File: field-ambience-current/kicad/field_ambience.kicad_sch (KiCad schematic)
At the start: 0 parts

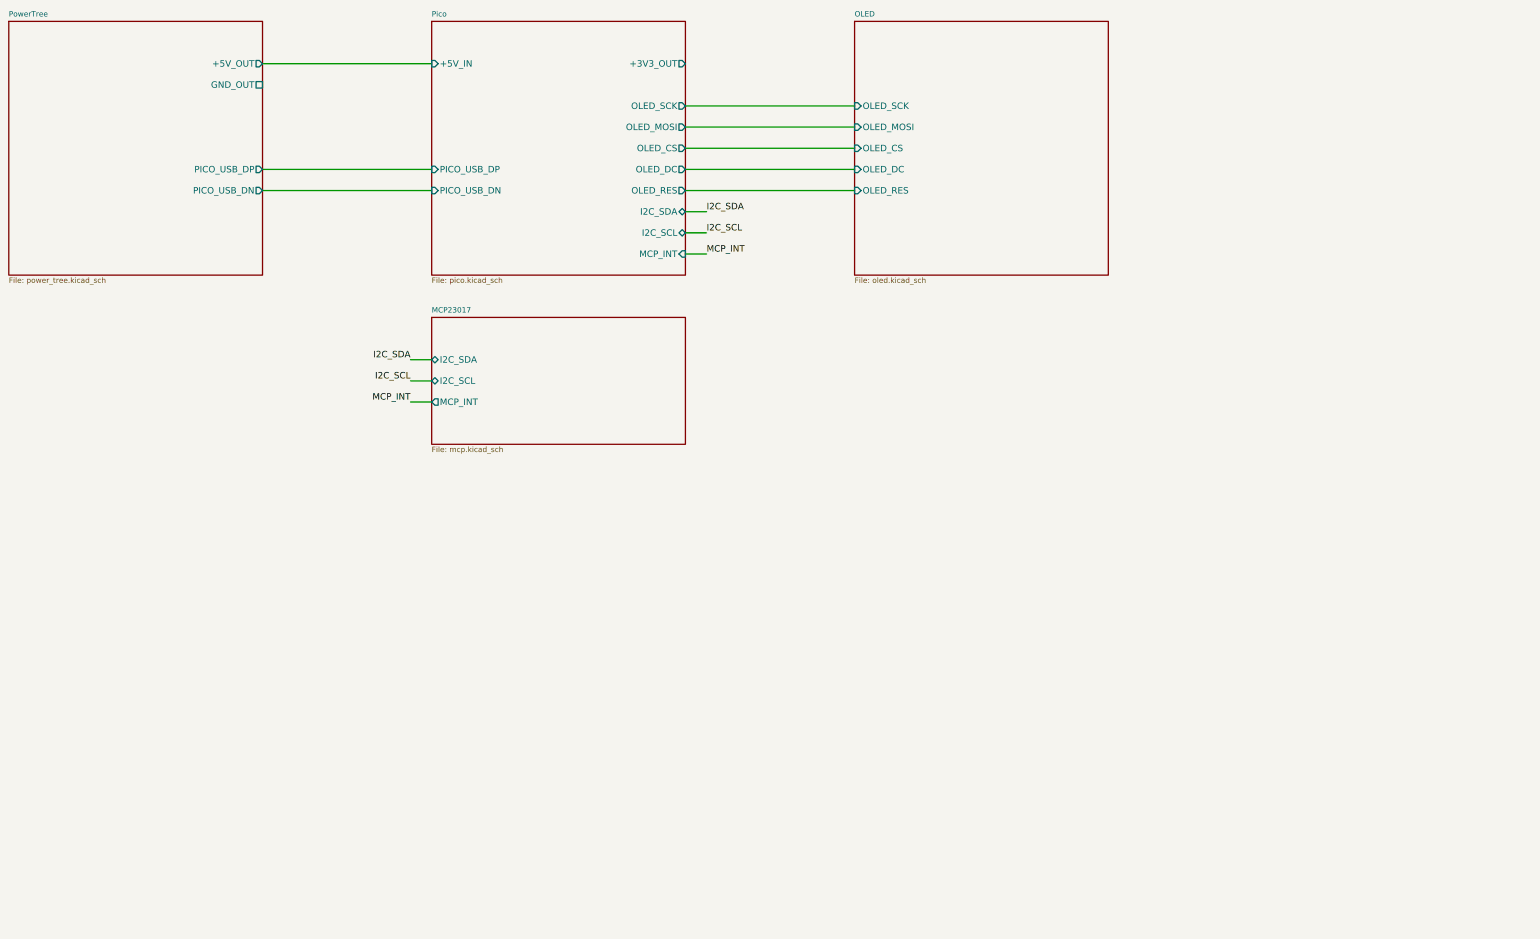
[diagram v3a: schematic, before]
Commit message: Add Sheet 5 (4x EC11 Encoder + RC-Debounce) per SPEC v0.6 §5/§M4
4 EC11-Encoder mit Push-Switch + Pull-Ups + Debounce-Caps:
- EN1 Drive (GP10/11/12)
- EN2 Brightness (GP13/14/15)
- EN3 Display (GP16/17/18)
- EN4 Volume (GP19/20/21)

Per encoder:
- A-Pin: R pull-up 10k zu +3V3, C debounce 100nF zu GND (v0.6 M4 Fix)
- B-Pin: R pull-up 10k, C debounce 100nF
- C-Pin: direkt zu GND (Common)
- SW1-Pin: R pull-up 10k, Hier-Output zu Pico
- SW2-Pin: direkt zu GND

BOM Sheet 5: 12× R 10k (8 für A/B-Pull-Ups R7-R14 + 4 für SW R15-R18),
8× C 100nF (Debounce C10-C17), 4× EC11 Encoder.

Root sheet umstrukturiert für Layout-Platz:
- Pico-Box erweitert von (60, 60) auf (60, 130) für 12 zusätzliche
  Encoder-Pins auf rechter Seite (y=110-165)
- MCP-Box von (130, 110) nach (130, 200) verschoben um Pico-Expansion
  Platz zu machen; I2C/INT-Labels entsprechend bei y=210-220 jetzt
- Encoder-Box bei (230, 105) size (60, 70) mit 12 input pins
- 12 direkte Wires Pico→Encoder bei y=110-165

Analyzer: 0 funktionale Errors (3 VM-001 false-positives unverändert),
23 warnings (von 35 gefallen, da Encoder-Signale jetzt 2-pin nets sind).
61 components total, 70 nets, 16 caps + 20 resistors + 16 switches.

Alle 4 EN1-EN4 pin_nets verifiziert via analyzer:
  Pin 1 (A): correct net (DRIVE_A / BRIGHT_A / DISPLAY_A / VOL_A)
  Pin 2 (B): correct net
  Pin 3 (C): GND
  Pin 4 (SW1): correct SW net
  Pin 5 (SW2): GND
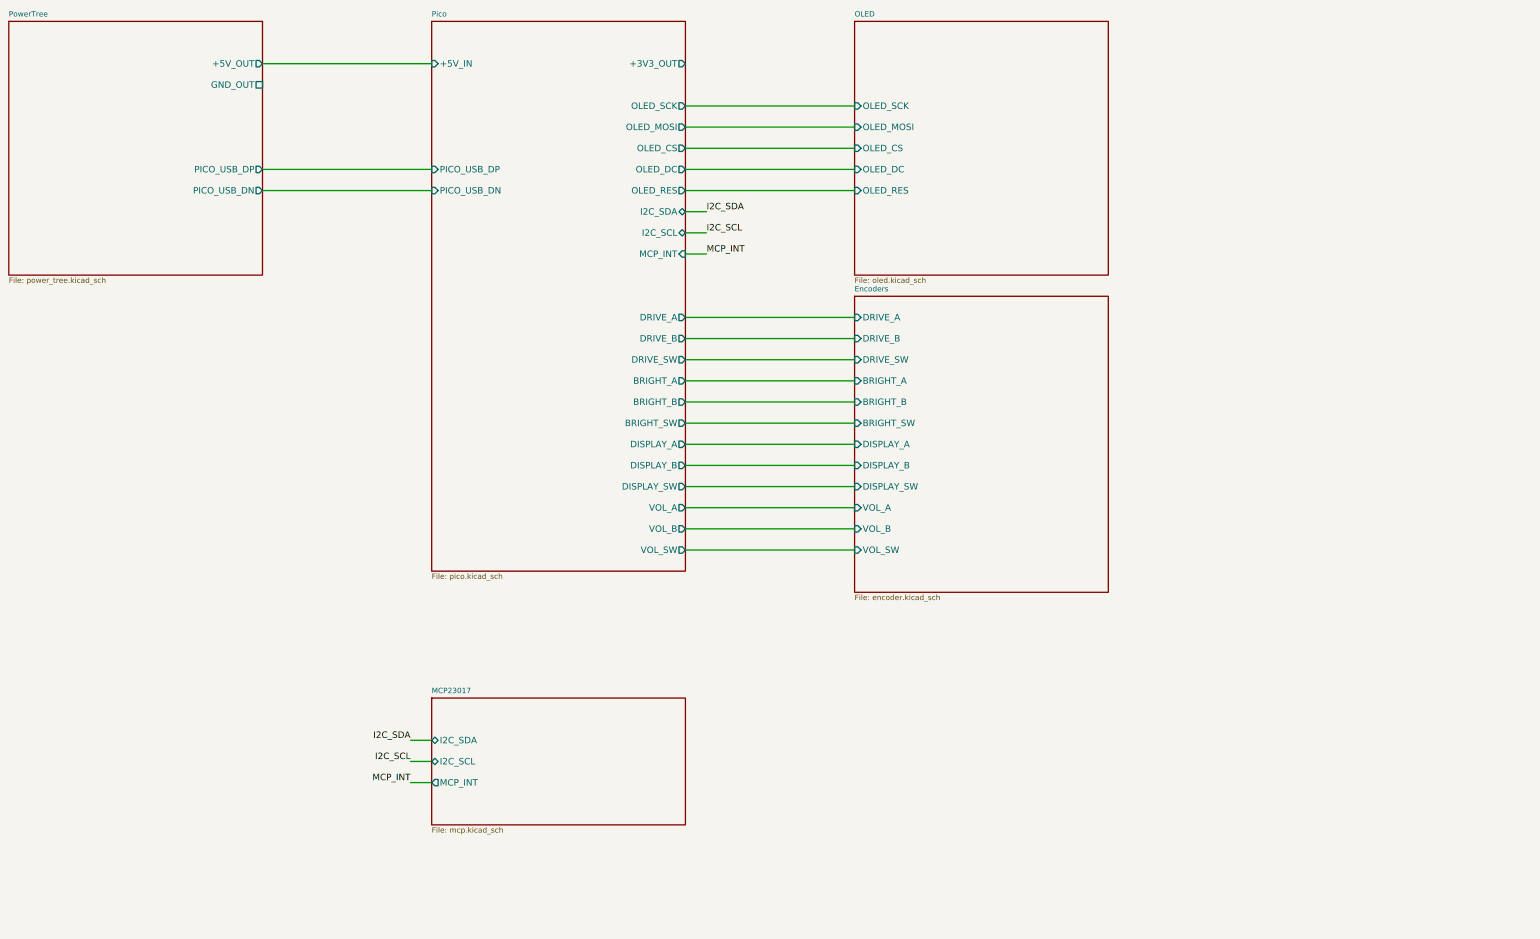
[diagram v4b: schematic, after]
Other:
- added sheet Encoders (encoder.kicad_sch)
- sheet Pico ports: added BRIGHT_A, BRIGHT_B, BRIGHT_SW, DISPLAY_A, DISPLAY_B, DISPLAY_SW, DRIVE_A, DRIVE_B, DRIVE_SW, VOL_A, VOL_B, VOL_SW; removed none
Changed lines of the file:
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@@
       (effects (font (size 1.524 1.524)) (justify right))
 ))
-  (sheet (at 130 40) (size 60 60) (fields_autoplaced)
+  (sheet (at 130 40) (size 60 130) (fields_autoplaced)
     (stroke (width 0.1524) (type solid))
     (fill (color 0 0 0 0.0000))
     (property "Sheetname" "Pico" (at 130 39 0)
       (effects (font (size 1.27 1.27)) (justify left bottom)))
-    (property "Sheetfile" "pico.kicad_sch" (at 130 100.5 0)
+    (property "Sheetfile" "pico.kicad_sch" (at 130 170.5 0)
       (effects (font (size 1.27 1.27)) (justify left top)))
     (pin "+5V_IN" input (at 130 50 180)
@@
     (pin "MCP_INT" input (at 190 95 0)
       (effects (font (size 1.524 1.524)) (justify right))
+)
+    (pin "DRIVE_A" output (at 190 110 0)
+      (effects (font (size 1.524 1.524)) (justify right))
+)
+    (pin "DRIVE_B" output (at 190 115 0)
+      (effects (font (size 1.524 1.524)) (justify right))
+)
+    (pin "DRIVE_SW" output (at 190 120 0)
+      (effects (font (size 1.524 1.524)) (justify right))
+)
+    (pin "BRIGHT_A" output (at 190 125 0)
+      (effects (font (size 1.524 1.524)) (justify right))
+)
+    (pin "BRIGHT_B" output (at 190 130 0)
+      (effects (font (size 1.524 1.524)) (justify right))
+)
+    (pin "BRIGHT_SW" output (at 190 135 0)
+      (effects (font (size 1.524 1.524)) (justify right))
+)
+    (pin "DISPLAY_A" output (at 190 140 0)
+      (effects (font (size 1.524 1.524)) (justify right))
+)
+    (pin "DISPLAY_B" output (at 190 145 0)
+      (effects (font (size 1.524 1.524)) (justify right))
+)
+    (pin "DISPLAY_SW" output (at 190 150 0)
+      (effects (font (size 1.524 1.524)) (justify right))
+)
+    (pin "VOL_A" output (at 190 155 0)
+      (effects (font (size 1.524 1.524)) (justify right))
+)
+    (pin "VOL_B" output (at 190 160 0)
+      (effects (font (size 1.524 1.524)) (justify right))
+)
+    (pin "VOL_SW" output (at 190 165 0)
+      (effects (font (size 1.524 1.524)) (justify right))
 ))
   (sheet (at 230 40) (size 60 60) (fields_autoplaced)
@@
       (effects (font (size 1.524 1.524)) (justify left))
 ))
-  (sheet (at 130 110) (size 60 30) (fields_autoplaced)
+  (sheet (at 130 200) (size 60 30) (fields_autoplaced)
     (stroke (width 0.1524) (type solid))
     (fill (color 0 0 0 0.0000))
-    (property "Sheetname" "MCP23017" (at 130 109 0)
+    (property "Sheetname" "MCP23017" (at 130 199 0)
       (effects (font (size 1.27 1.27)) (justify left bottom)))
-    (property "Sheetfile" "mcp.kicad_sch" (at 130 140.5 0)
+    (property "Sheetfile" "mcp.kicad_sch" (at 130 230.5 0)
       (effects (font (size 1.27 1.27)) (justify left top)))
-    (pin "I2C_SDA" bidirectional (at 130 120 180)
+    (pin "I2C_SDA" bidirectional (at 130 210 180)
       (effects (font (size 1.524 1.524)) (justify left))
 )
-    (pin "I2C_SCL" bidirectional (at 130 125 180)
+    (pin "I2C_SCL" bidirectional (at 130 215 180)
       (effects (font (size 1.524 1.524)) (justify left))
 )
-    (pin "MCP_INT" output (at 130 130 180)
+    (pin "MCP_INT" output (at 130 220 180)
+      (effects (font (size 1.524 1.524)) (justify left))
+))
+  (sheet (at 230 105) (size 60 70) (fields_autoplaced)
+    (stroke (width 0.1524) (type solid))
+    (fill (color 0 0 0 0.0000))
+    (property "Sheetname" "Encoders" (at 230 104 0)
+      (effects (font (size 1.27 1.27)) (justify left bottom)))
+    (property "Sheetfile" "encoder.kicad_sch" (at 230 175.5 0)
+      (effects (font (size 1.27 1.27)) (justify left top)))
+    (pin "DRIVE_A" input (at 230 110 180)
+      (effects (font (size 1.524 1.524)) (justify left))
+)
+    (pin "DRIVE_B" input (at 230 115 180)
+      (effects (font (size 1.524 1.524)) (justify left))
+)
+    (pin "DRIVE_SW" input (at 230 120 180)
+      (effects (font (size 1.524 1.524)) (justify left))
+)
+    (pin "BRIGHT_A" input (at 230 125 180)
+      (effects (font (size 1.524 1.524)) (justify left))
+)
+    (pin "BRIGHT_B" input (at 230 130 180)
+      (effects (font (size 1.524 1.524)) (justify left))
+)
+    (pin "BRIGHT_SW" input (at 230 135 180)
+      (effects (font (size 1.524 1.524)) (justify left))
+)
+    (pin "DISPLAY_A" input (at 230 140 180)
+      (effects (font (size 1.524 1.524)) (justify left))
+)
+    (pin "DISPLAY_B" input (at 230 145 180)
+      (effects (font (size 1.524 1.524)) (justify left))
+)
+    (pin "DISPLAY_SW" input (at 230 150 180)
+      (effects (font (size 1.524 1.524)) (justify left))
+)
+    (pin "VOL_A" input (at 230 155 180)
+      (effects (font (size 1.524 1.524)) (justify left))
+)
+    (pin "VOL_B" input (at 230 160 180)
+      (effects (font (size 1.524 1.524)) (justify left))
+)
+    (pin "VOL_SW" input (at 230 165 180)
       (effects (font (size 1.524 1.524)) (justify left))
 ))
@@
   (wire (pts (xy 190 95) (xy 195 95)) (stroke (width 0) (type default)))
   (label "MCP_INT" (at 195 95 0) (effects (font (size 1.524 1.524)) (justify left bottom)))
-  (wire (pts (xy 125 120) (xy 130 120)) (stroke (width 0) (type default)))
-  (label "I2C_SDA" (at 125 120 0) (effects (font (size 1.524 1.524)) (justify right bottom)))
-  (wire (pts (xy 125 125) (xy 130 125)) (stroke (width 0) (type default)))
-  (label "I2C_SCL" (at 125 125 0) (effects (font (size 1.524 1.524)) (justify right bottom)))
-  (wire (pts (xy 125 130) (xy 130 130)) (stroke (width 0) (type default)))
-  (label "MCP_INT" (at 125 130 0) (effects (font (size 1.524 1.524)) (justify right bottom)))
+  (wire (pts (xy 125 210) (xy 130 210)) (stroke (width 0) (type default)))
+  (label "I2C_SDA" (at 125 210 0) (effects (font (size 1.524 1.524)) (justify right bottom)))
+  (wire (pts (xy 125 215) (xy 130 215)) (stroke (width 0) (type default)))
+  (label "I2C_SCL" (at 125 215 0) (effects (font (size 1.524 1.524)) (justify right bottom)))
+  (wire (pts (xy 125 220) (xy 130 220)) (stroke (width 0) (type default)))
+  (label "MCP_INT" (at 125 220 0) (effects (font (size 1.524 1.524)) (justify right bottom)))
+  (wire (pts (xy 190 110) (xy 230 110)) (stroke (width 0) (type default)))
+  (wire (pts (xy 190 115) (xy 230 115)) (stroke (width 0) (type default)))
+  (wire (pts (xy 190 120) (xy 230 120)) (stroke (width 0) (type default)))
+  (wire (pts (xy 190 125) (xy 230 125)) (stroke (width 0) (type default)))
+  (wire (pts (xy 190 130) (xy 230 130)) (stroke (width 0) (type default)))
+  (wire (pts (xy 190 135) (xy 230 135)) (stroke (width 0) (type default)))
+  (wire (pts (xy 190 140) (xy 230 140)) (stroke (width 0) (type default)))
+  (wire (pts (xy 190 145) (xy 230 145)) (stroke (width 0) (type default)))
+  (wire (pts (xy 190 150) (xy 230 150)) (stroke (width 0) (type default)))
+  (wire (pts (xy 190 155) (xy 230 155)) (stroke (width 0) (type default)))
+  (wire (pts (xy 190 160) (xy 230 160)) (stroke (width 0) (type default)))
+  (wire (pts (xy 190 165) (xy 230 165)) (stroke (width 0) (type default)))
   (sheet_instances
     (path "/" (page "1")))

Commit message: Add Sheet 6 (Audio) per SPEC v0.6 §8 + H2/M2/C2 Fixes
U3 PCM5102A (TSSOP-20, C107671) I²S DAC:
- Pin 1-3: I2S_LRCK/BCK/DOUT ← hier-inputs (von Sheet 7 Pi-Header später)
- 3-wire mode: SCK (pin 18) → GND (internal PLL aus BCK)
- FMT (8) → GND I²S mode, FLT (5) → GND, DEMP (6) → GND
- XSMT (7) → R_XSMT 10k pull-up zu +3V3 (un-muted by default)
- VCOM (14): C_VCOM 1µF filter, VNEG (11): C_VNEG 1µF filter
- CPVDD (13): C_CPVDD 10µF + 100nF (charge pump supply)
- DVDD (19): C8a 10µF + C8b 100nF (digital)
- AVDD (15): via FB1 BLM18AG601 + C7a 10µF + C7b 100nF (v0.6 M2 Fix)
- VOUTL (9), VOUTR (16) → coupling zu PAM8403

FB1 BLM18AG601 (C19330) Ferrit-Bead zwischen +3V3 und AVDD-Pin.

U4 PAM8403 (SOP-16, C17337) Class-D Stereo Amp:
- VDD (1, 15, 16) → +5V mit C9 10µF + C9b 100nF lokal (v0.6 H2 Fix)
- SHDN (3) ← AMP_SHUTDOWN von Pico GP27 (v0.6 C2 Fix Pop-Suppression)
- MUTE (4) ← AMP_MUTE von Pico GP28 (v0.6 C2 Fix)
- INL+ (5) ← C_in_L 1µF DC-block + R_VOL_L 10k series ← PCM_VOUTL
- INR+ (7) ← C_in_R 1µF DC-block + R_VOL_R 10k series ← PCM_VOUTR
- INL-/INR- (6/8) → GND (single-ended, internal bias)
- OUTL+/- (9/10) → J6 Speaker L (PUI AS04008PS 4Ω/4W BTL)
- OUTR+/- (11/12) → J7 Speaker R (PUI AS04008PS 4Ω/4W BTL)

Note: PAM8403 pinout variiert zwischen Herstellern. Vor PCB-Layout
gegen tatsächliches Datasheet von JLC-stockable PAM8403 (C17337)
verifizieren. KiCad-Symbol nutzt logisches Pinout.

Root sheet: Audio-Sheet bei (230, 200) size (60, 50) mit 5 input pins.
Pico-Sheet bekommt AMP_SHUTDOWN/AMP_MUTE outputs auf linker Seite.
Label-bridges für AMP_SHDN, AMP_MUTE, I2S_BCK/LRCK/DOUT.
I2S-Signale bleiben momentan dangling (Sheet 7 Pi-Header noch nicht
implementiert).

Analyzer: 0 functional errors (3 VM-001 false positives unverändert).
24 warnings, 81 components, 86 nets total. U3+U4 pin_nets verifiziert.
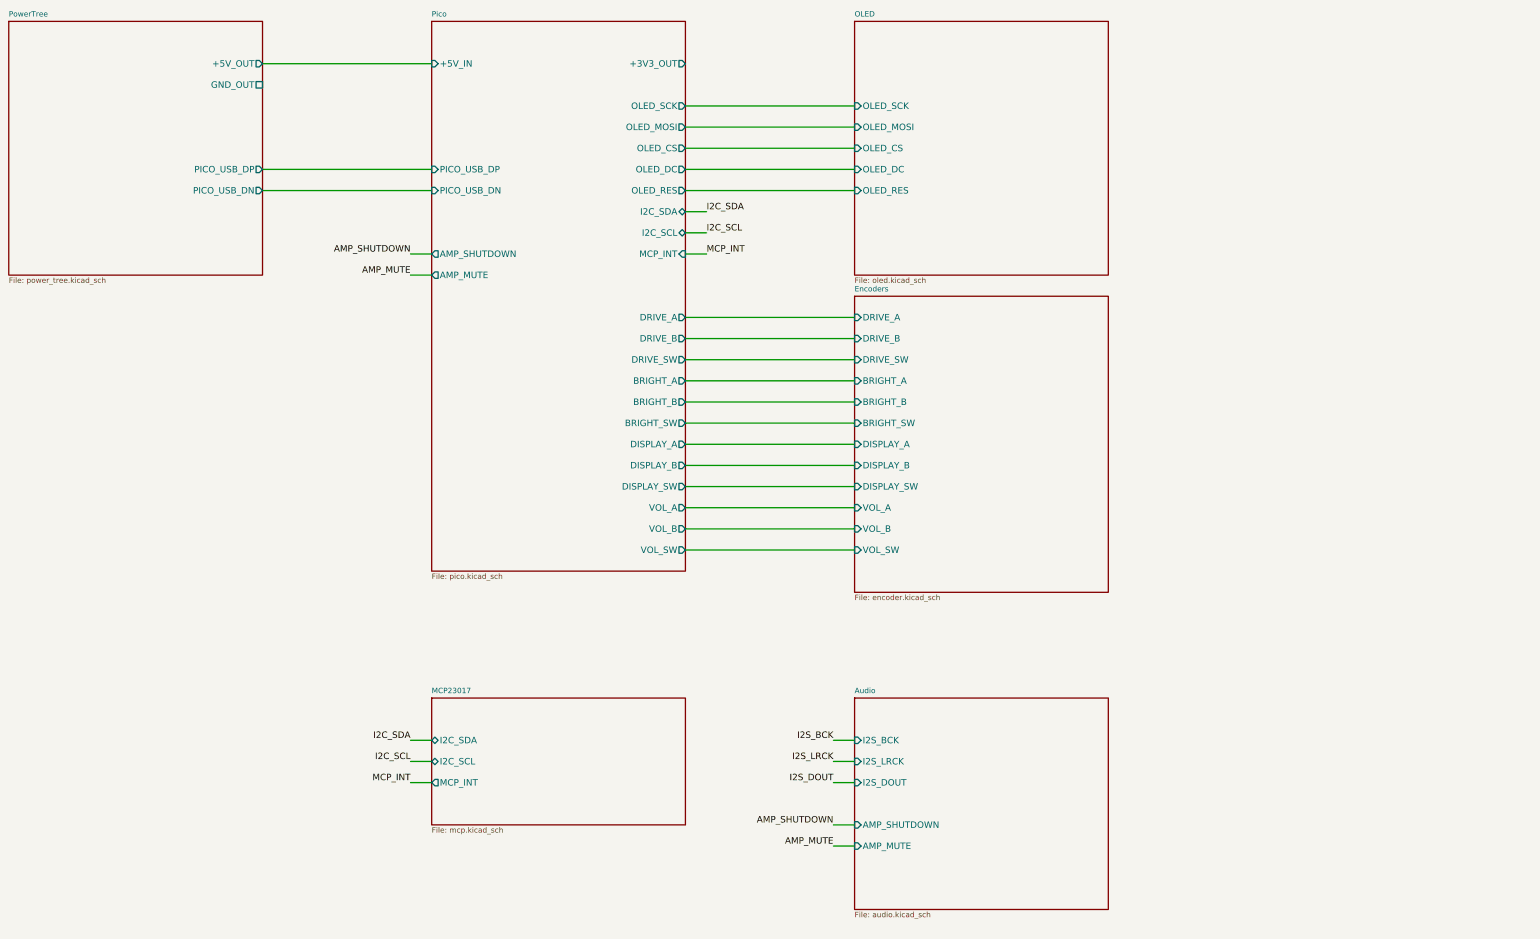
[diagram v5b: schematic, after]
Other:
- added sheet Audio (audio.kicad_sch)
- sheet Pico ports: added AMP_MUTE, AMP_SHUTDOWN; removed none
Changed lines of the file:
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@@
     (pin "VOL_SW" output (at 190 165 0)
       (effects (font (size 1.524 1.524)) (justify right))
+)
+    (pin "AMP_SHUTDOWN" output (at 130 95 180)
+      (effects (font (size 1.524 1.524)) (justify left))
+)
+    (pin "AMP_MUTE" output (at 130 100 180)
+      (effects (font (size 1.524 1.524)) (justify left))
 ))
   (sheet (at 230 40) (size 60 60) (fields_autoplaced)
@@
   (wire (pts (xy 125 220) (xy 130 220)) (stroke (width 0) (type default)))
   (label "MCP_INT" (at 125 220 0) (effects (font (size 1.524 1.524)) (justify right bottom)))
+  (sheet (at 230 200) (size 60 50) (fields_autoplaced)
+    (stroke (width 0.1524) (type solid))
+    (fill (color 0 0 0 0.0000))
+    (property "Sheetname" "Audio" (at 230 199 0)
+      (effects (font (size 1.27 1.27)) (justify left bottom)))
+    (property "Sheetfile" "audio.kicad_sch" (at 230 250.5 0)
+      (effects (font (size 1.27 1.27)) (justify left top)))
+    (pin "I2S_BCK" input (at 230 210 180)
+      (effects (font (size 1.524 1.524)) (justify left))
+)
+    (pin "I2S_LRCK" input (at 230 215 180)
+      (effects (font (size 1.524 1.524)) (justify left))
+)
+    (pin "I2S_DOUT" input (at 230 220 180)
+      (effects (font (size 1.524 1.524)) (justify left))
+)
+    (pin "AMP_SHUTDOWN" input (at 230 230 180)
+      (effects (font (size 1.524 1.524)) (justify left))
+)
+    (pin "AMP_MUTE" input (at 230 235 180)
+      (effects (font (size 1.524 1.524)) (justify left))
+))
+  (wire (pts (xy 125 95) (xy 130 95)) (stroke (width 0) (type default)))
+  (label "AMP_SHUTDOWN" (at 125 95 0) (effects (font (size 1.524 1.524)) (justify right bottom)))
+  (wire (pts (xy 125 100) (xy 130 100)) (stroke (width 0) (type default)))
+  (label "AMP_MUTE" (at 125 100 0) (effects (font (size 1.524 1.524)) (justify right bottom)))
+  (wire (pts (xy 225 230) (xy 230 230)) (stroke (width 0) (type default)))
+  (label "AMP_SHUTDOWN" (at 225 230 0) (effects (font (size 1.524 1.524)) (justify right bottom)))
+  (wire (pts (xy 225 235) (xy 230 235)) (stroke (width 0) (type default)))
+  (label "AMP_MUTE" (at 225 235 0) (effects (font (size 1.524 1.524)) (justify right bottom)))
+  (wire (pts (xy 225 210) (xy 230 210)) (stroke (width 0) (type default)))
+  (label "I2S_BCK" (at 225 210 0) (effects (font (size 1.524 1.524)) (justify right bottom)))
+  (wire (pts (xy 225 215) (xy 230 215)) (stroke (width 0) (type default)))
+  (label "I2S_LRCK" (at 225 215 0) (effects (font (size 1.524 1.524)) (justify right bottom)))
+  (wire (pts (xy 225 220) (xy 230 220)) (stroke (width 0) (type default)))
+  (label "I2S_DOUT" (at 225 220 0) (effects (font (size 1.524 1.524)) (justify right bottom)))
   (wire (pts (xy 190 110) (xy 230 110)) (stroke (width 0) (type default)))
   (wire (pts (xy 190 115) (xy 230 115)) (stroke (width 0) (type default)))
